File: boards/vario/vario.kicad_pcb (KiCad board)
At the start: 2 copper layers, 90 x 100 mm, 121 parts, among them J1 Conn_02x20_Odd_Even, J2 SD_Card, J3 Mini-DIN-6, Q1 2N7002, Q2 2N7002, Q3 2N7002, Q4 2N7002, Q5 2N7002, U1 74HC273PW, U10 74HC161PW, U11 MC74HC244ADT, U12 74HC74PW, U13 74HC74PW, U14 74HC08PW, U15 74HC74PW, U16 74HC74PW, U17 74HC161PW, U18 74HC273PW, U19 CD74HC280MT, U2 74HC161PW, U20 MC74HC151ADTR2G, U21 MC74HC151ADTR2G, U22 MC74HC244ADT, U23 CD74HC280MT, U24 SN74LV10APW, U25 74HC08PW, U26 74HC04PW, U27 74HC30D, U28 SN74HC32PWR, U29 SN74HC32PWR, U3 74HC74PW, U30 SN74HC32PWR, U31 SN74LV14APW, U32 SN74HC32PWR, U33 74HC08PW, U34 74HC273PW, U35 MC74HC244ADT, U36 IFX54441EJV33, U37 SN74HC139PW, U38 SN74HC32PWR, U4 74HC273PW, U5 MC74HC151ADTR2G, U6 MC74HC244ADT, U7 SN74LV14APW, U8 74HC273PW, U9 74HC273PW

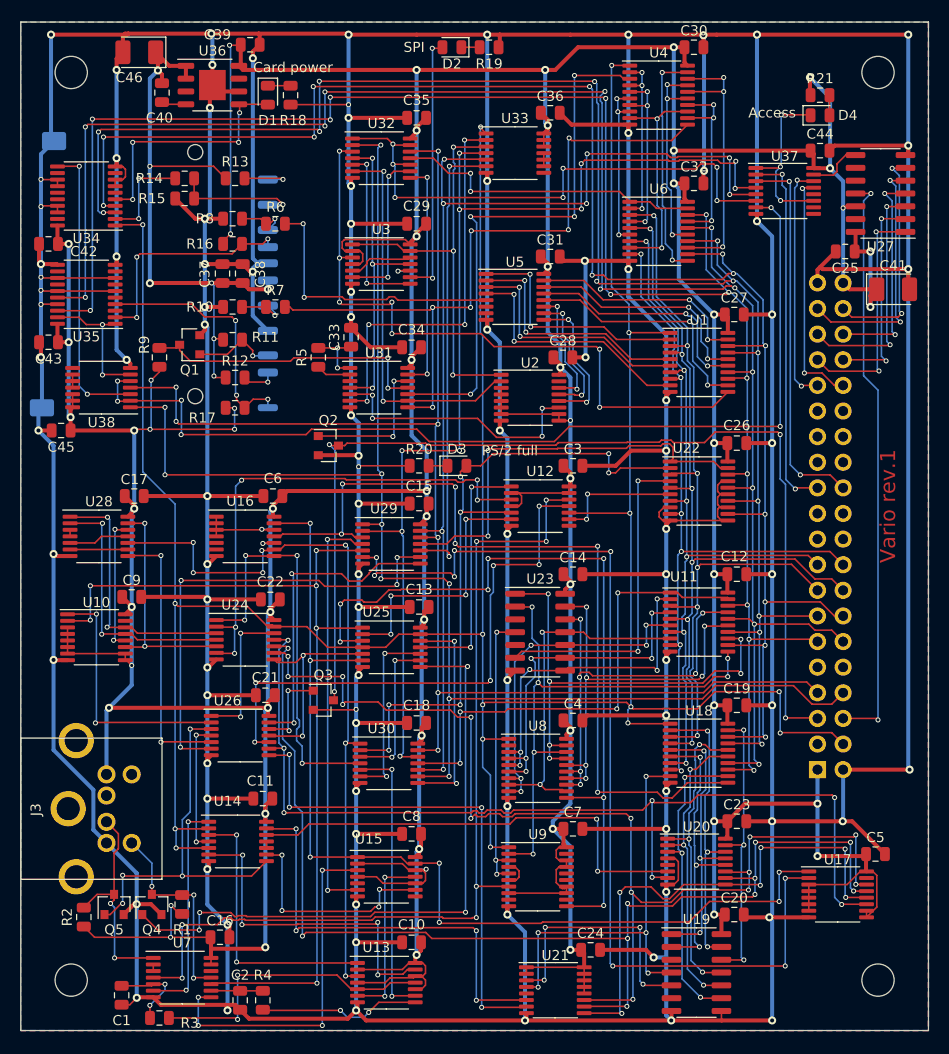
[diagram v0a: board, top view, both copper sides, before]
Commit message: Vario: move crosstalk-sensitive traces
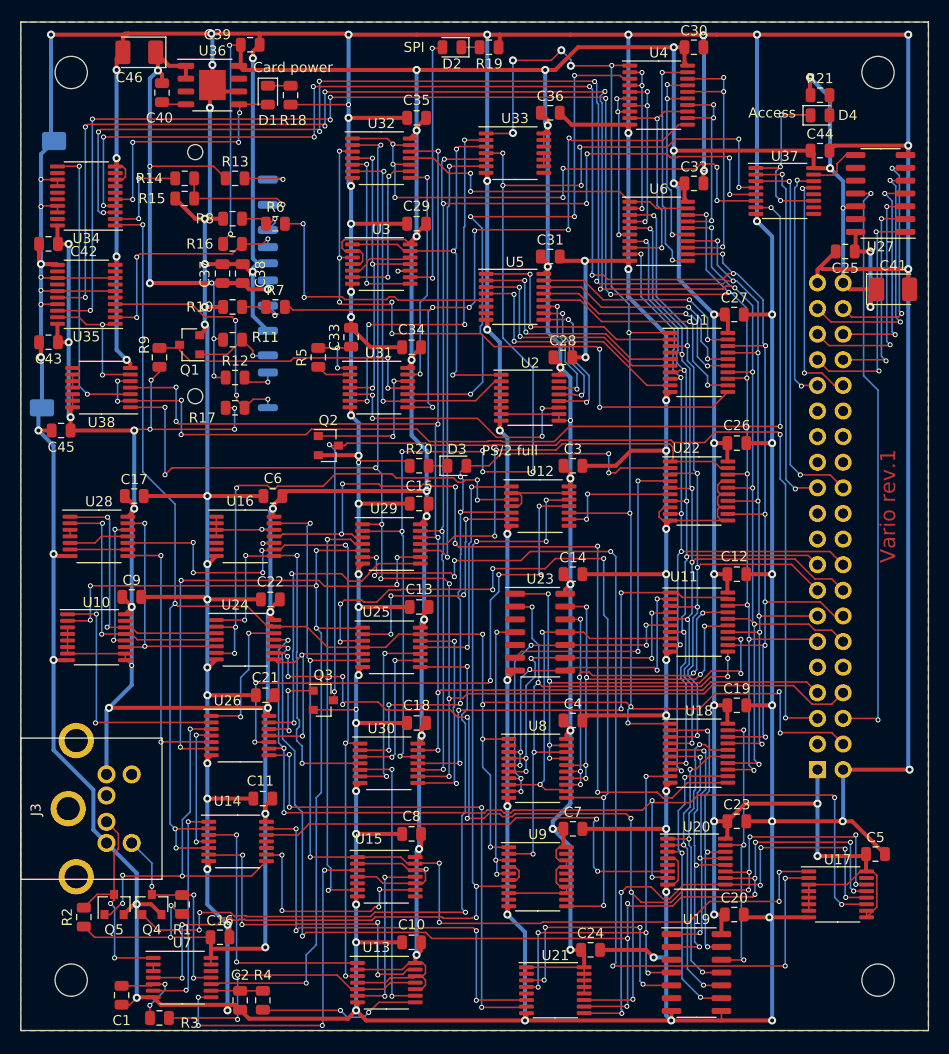
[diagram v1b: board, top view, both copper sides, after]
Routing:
- net ~rst: track 306.2 -> 276.4 mm, vias 16 -> 19
- net /~ps2_data_sel: track 111.2 -> 120.0 mm, vias 10 -> 12
- net /SPI/miso: track 54.3 -> 54.9 mm
- net /ps2/~clk_out: track 64.0 -> 64.5 mm

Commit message: Vario: rectangular pads on the board
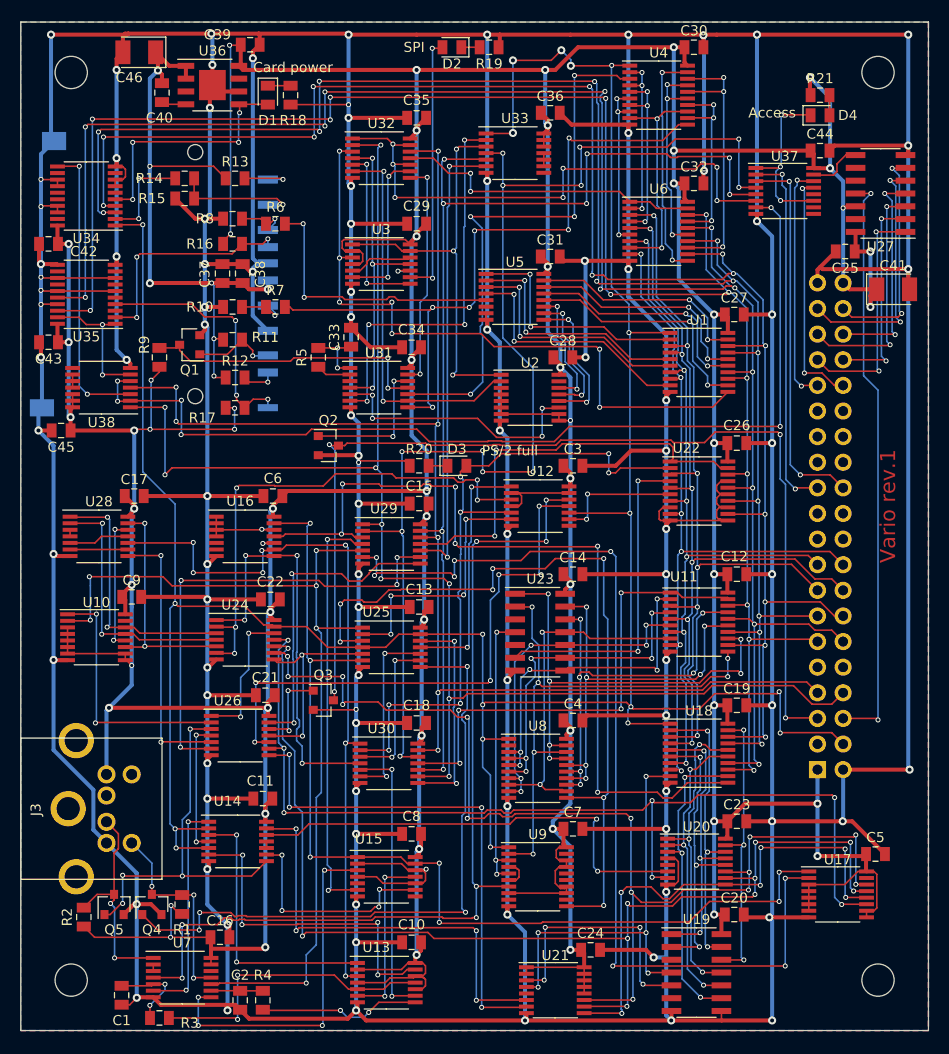
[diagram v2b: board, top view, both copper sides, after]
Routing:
- net /ps2/recv_clk: track 90.5 -> 91.9 mm
- net VCC: track 811.3 -> 812.5 mm
- net GND: track 1240.2 -> 1240.8 mm
